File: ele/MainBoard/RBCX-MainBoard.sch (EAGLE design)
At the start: 311 parts, among them IC1 AMS1117-3.3, IC10 INA180A4, IC11 INA180A4, IC2 DRV8833PWP, IC3 INA180A4, IC4 INA180A4, IC5 DRV8833PWP, IC6 INA180A4, IC7 INA180A4, IC8 INA180A4, IC9 INA180A4, Q1 NCE20P45Q, Q10 2N7002, Q11 2N7002, Q2 NCE20P45Q, Q3 2N7002, Q4 2N7002, Q5 2N7002, Q6 2N7002, Q7 2N7002, Q8 2N7002, Q9 2N7002, SW1 CHOOSE_ME, SW2 CHOOSE_ME, SW3 CHOOSE_ME, SW4 CHOOSE_ME, SW5 CHOOSE_ME, SW6 CHOOSE_ME, U1 STM32F103VCT6, X1 POWER_OUT, X10 52745-3090, X11 52745-2090, X2 POWER_IN, Y1 5032/2P, Y2 3215_2P

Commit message: MainBoard: Add BOM, update parts value and package
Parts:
- removed C50: 10n, rcl_upravena:C-EUC0603
- removed C51: 1n, rcl_upravena:C-EUC0603
- removed C52, C54: 18p, rcl_upravena:C-EUC0603
- removed C53, C55: 6p, rcl_upravena:C-EUC0603
- removed C57: 10u, rcl_upravena:C-EUC0805
- removed JP56: ESP_I2C1, pinhead:PINHD-1X4
- removed JP57: ESP_SPI_AUX3, pinhead:PINHD-1X3
- removed JP58: +3V3STM, pinhead:PINHD-2X4
- removed JP59: ESP_I2C_AUX1, pinhead:PINHD-1X3
- removed JP60: +3V3, pinhead:PINHD-2X4
- removed JP61: +5V, pinhead:PINHD-2X4
- removed JP62: ESP_I2C2, pinhead:PINHD-1X4
- removed JP63: VCC, pinhead:PINHD-2X4
- removed JP64: ESP_I2C_AUX2, pinhead:PINHD-1X3
- removed JP66: ILED, pinhead:PINHD-1X3
- removed R119, R120, R125, R131, R132, R134: 4k7, rcl_upravena:R-EU_R0402
- removed R121, R122, R123, R124, R127, R128, R133: 180R, rcl_upravena:R-EU_R0402
- removed R126, R129: 100k, rcl_upravena:R-EU_R0402
- removed SJ8: (no value), jumper:SJ2W
- added C1, C6: 10u, rcl_upravena:C-EUC0805
- added C11: 10n, rcl_upravena:C-EUC0402
- added C17: 2u2, rcl_upravena:C-EUC0603
- added C23: 220u, rcl_upravena:CPOL-EUE5-10.5
- added C24, C25, C26: 100n, rcl_upravena:C-EUC0402
- added JP22: BOOT_SW, pinhead:PINHD-1X2
- added JP25: UTS2, pinhead:PINHD-1X4
- added JP31: ESP_SPI1, pinhead:PINHD-1X6
- added JP33: ESP_UART_AUX, pinhead:PINHD-1X3
- added JP34: ESP_I2C_AUX1_5V, pinhead:PINHD-1X3
- added JP35: ESP_SPI_AUX1, pinhead:PINHD-1X3
- added JP36: ESP_I2C2_5V, pinhead:PINHD-1X4
- added JP37: ESP_SPI2, pinhead:PINHD-1X6
- added JP38: ESP_UCOM, pinhead:PINHD-1X4
- added JP39: ESP_I2C_AUX2_5V, pinhead:PINHD-1X3
- added R70, R71, R72, R73, R74, R82, R84, R85, R89, R90, R91, R92, R94, R95: 330R, rcl_upravena:R-EU_R0402
- added R86: 4k7, rcl_upravena:R-EU_R0402
- added SJ3: (no value), jumper:SJ2W
- C10: value 2u2 -> 10u; device rcl_upravena:C-EUC0603 -> rcl_upravena:C-EUC0805; VOLTAGE 16V -> 25V
- C12: value 10u -> 2u2; device rcl_upravena:C-EUC0805 -> rcl_upravena:C-EUC0603; VOLTAGE 25V -> 16V
- C13, C19: device rcl_upravena:C-EUC0603 -> rcl_upravena:C-EUC0402; VOLTAGE 25V -> 16V
- C14: value 2u2 -> 100n; device rcl_upravena:C-EUC0805 -> rcl_upravena:C-EUC0402
- C15, C32, C33, C34, C44: value 100n -> 10u; device rcl_upravena:C-EUC0603 -> rcl_upravena:C-EUC0805; VOLTAGE 16V -> 25V
- C16: value 100n -> 10n; device rcl_upravena:C-EUC0603 -> rcl_upravena:C-EUC0402; VOLTAGE 16V -> 25V
- C18: value 10u -> 100n; device rcl_upravena:C-EUC0805 -> rcl_upravena:C-EUC0402; VOLTAGE 25V -> 16V
- C2: value 22u -> 10u; device rcl_upravena:CPOL-EUB/3528-21R -> rcl_upravena:C-EUC0805; DIELECTRIC (none) -> X5R; VOLTAGE 16V -> 25V
- C20: value 2u2 -> 220u; device rcl_upravena:C-EUC0805 -> rcl_upravena:CPOL-EUE5-10.5; DIELECTRIC X5R -> (none)
- C21, C22: value 100n -> 220u; device rcl_upravena:C-EUC0603 -> rcl_upravena:CPOL-EUE5-10.5; DIELECTRIC X5R -> (none)
- C27, C43: value 220u -> 100n; device rcl_upravena:CPOL-EUE5-10.5 -> rcl_upravena:C-EUC0402; DIELECTRIC (none) -> X5R
- C28, C29, C30: value 220u -> 1u; device rcl_upravena:CPOL-EUE5-10.5 -> rcl_upravena:C-EUC0402; DIELECTRIC (none) -> X5R
- C3, C42: VOLTAGE 16V -> 25V
- C31: value 100n -> 1u; device rcl_upravena:C-EUC0603 -> rcl_upravena:C-EUC0402
- C35: value 1u -> 10u; device rcl_upravena:C-EUC0603 -> rcl_upravena:C-EUC0805; VOLTAGE 16V -> 25V
- C36: value 1u -> 220u; device rcl_upravena:C-EUC0603 -> rcl_upravena:CPOL-EUE5-10.5; DIELECTRIC X5R -> (none)
- C37, C38: value 1u -> 100n; device rcl_upravena:C-EUC0603 -> rcl_upravena:C-EUC0402
- C39, C40, C41: value 10u -> 100n; device rcl_upravena:C-EUC0805 -> rcl_upravena:C-EUC0402
- C45, C47: value 100n -> 18p; device rcl_upravena:C-EUC0603 -> rcl_upravena:C-EUC0402; DIELECTRIC X5R -> np0; VOLTAGE 16V -> 50V
- C46, C48: value 100n -> 6.8p; device rcl_upravena:C-EUC0603 -> rcl_upravena:C-EUC0402; DIELECTRIC X5R -> np0; VOLTAGE 16V -> 50V
- C49: value 4u7 -> 10u; VOLTAGE 16V -> 25V
- C8: value 10u -> 1u; device rcl_upravena:C-EUC0805 -> rcl_upravena:C-EUC0402
- C9: value 1u -> 2u2
- IC3, IC4, IC6, IC7: DESCRIPTION PMIC - CURRENT & POWER MONITORS & REGULATORS 1 200 V/V ±0.1% 105KHZ -0.2V ~ 26V 2.7V ~ 5.5V SOT-23-5 ROHS -> PMIC - CURRENT & POWER MONITORS & REGULATORS 1 200 V/V ±0.1% 105KHZ -0.2V ~ 26V 2.7V ~ 5.5V SOT-23-5 ROHS
- JP1: value IM7_EN -> IM1_EN
- JP10: value IM1_EN -> IM2_EN
- JP11: value IM2_EN -> IM3_EN
- JP12: value IM3_EN -> IM4_EN
- JP13: value IM4_EN -> IM5_EN
- JP15: value SERVO1 -> SERVO2
- JP16: value SERVO1 -> SERVO3
- JP17: value SERVO1 -> SERVO4
- JP26: value BOOT_SW -> EXPANDER_UART; device pinhead:PINHD-1X2 -> pinhead:PINHD-1X3
- JP27: value UTS2 -> DEBUG
- JP28: value EXPANDER_UART -> UTS3; device pinhead:PINHD-1X3 -> pinhead:PINHD-1X4
- JP29: value DEBUG -> UTS4
- JP30: value UTS3 -> ESP_UART
- JP32: value UTS4 -> ESP_I2C1_5V
- JP43: value ESP_UART -> ESP_I2C1
- JP44: value ESP_SPI1 -> ESP_SPI_AUX3; device pinhead:PINHD-1X6 -> pinhead:PINHD-1X3
- JP45: value ESP_I2C1_5V -> +3V3STM; device pinhead:PINHD-1X4 -> pinhead:PINHD-2X4
- JP46: value ESP_UART_AUX -> ESP_I2C_AUX1
- JP47: value ESP_I2C_AUX1_5V -> +3V3; device pinhead:PINHD-1X3 -> pinhead:PINHD-2X4
- JP48: value ESP_SPI_AUX1 -> +5V; device pinhead:PINHD-1X3 -> pinhead:PINHD-2X4
- JP49: value ESP_I2C2_5V -> ESP_I2C2
- JP50: value ESP_SPI2 -> VCC; device pinhead:PINHD-1X6 -> pinhead:PINHD-2X4
- JP51: value ESP_UCOM -> ESP_I2C_AUX2; device pinhead:PINHD-1X4 -> pinhead:PINHD-1X3
- JP52: value ESP_I2C_AUX2_5V -> ILED
- LED1: value GREEN -> green; device led:LEDSML0603 -> led:LEDCHIP-LED0603
- LED2: value GREEN -> yellow; device led:LEDSML0603 -> led:LEDCHIP-LED0603
- LED3: value GREEN -> red; device led:LEDSML0603 -> led:LEDCHIP-LED0603
- LED4: value GREEN -> blue; device led:LEDSML0603 -> led:LEDCHIP-LED0603
- LED5: value green -> red
- LED6: value yellow -> red
- LED8: value blue -> red
- R10, R11: value 4k7 -> 10k
- R100, R101, R111, R112, R113, R87: value 180R -> 4k7
- R102, R103, R104, R108, R109, R114, R47, R48, R49, R50, R51, R64, R65, R67, R69, R75, R76, R77, R78, R79, R80, R81, R83, R88, R93, R96, R99: value 180R -> 330R
- R105: value 4k7 -> 330R
- R107, R110, R62, R63: value 180R -> 100k
- R13: value 4k7 -> 2k2
- R14, R15, R40: value 2k2 -> 1k
- R18, R19: value 8m -> 2k2; device rcl_upravena:R-EU_R1206S -> rcl_upravena:R-EU_R0402
- R2, R5: value 2M -> 10k
- R20, R21, R41: value 2k2 -> 5m; device rcl_upravena:R-EU_R0402 -> rcl_upravena:R-EU_R1206S
- R24, R25: value 10k -> 2k2
- R26, R27: value 8m -> 10k; device rcl_upravena:R-EU_R1206S -> rcl_upravena:R-EU_R0402
- R28, R29: value 0R -> 5m
- R32: value 1k -> 0R; device rcl_upravena:R-EU_R0402 -> rcl_upravena:R-EU_R1206S
- R33: value 5m -> 0R
- R4: value 100k -> 1M
- R44: device rcl_upravena:R-EU_R0603 -> rcl_upravena:R-EU_R0402
- R45, R46: value 180R -> 2k2
- R53: value 330R -> 100k
- R6: value 24k -> 100k
- R60, R61: value 100k -> 330R
- R66: value 10k -> 330R; device rcl_upravena:R-EU_R0603 -> rcl_upravena:R-EU_R0402
- R68: value 10k -> 330R
- R7: value 5k6 -> 1M
- R8: value 10k -> 24k
- R9: value 10k -> 5k6
- X5: value (none) -> uUSB
- renumbered J1 to X5, JP53 to JP40, JP54 to JP41, JP55 to JP42, R115 to R96, R116 to R97, R117 to R98, R118 to R99, SJ10 to SJ6, SJ11 to SJ7, SJ9 to SJ5, SW1 to S1, SW2 to S2, SW3 to S3, SW4 to S4, SW5 to S5, SW6 to S6, U1 to IC12, X10 to X3, X11 to X4
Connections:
- net +3V3: now also JP33.3, JP35.3, JP37.1, JP43.1, JP44.3, JP47.1, JP47.3, JP47.5, JP47.7, JP49.1, JP51.3, LED8.A, R100.2, R106.1, R107.1, R110.1, R111.1, R112.2, R86.2, SJ4.1; no longer JP48.3, JP50.1, JP56.1, JP57.3, JP59.3, JP60.1, JP60.3, JP60.5, JP60.7, JP62.1, JP64.3, LED4.A, R105.2, R119.2, R125.1, R126.1, R129.1, R131.1, R134.2, SJ8.1
- net +3V3S: now also C13.1, C14.1, C18.1, C19.1, C2.2, C24.1, C25.1, C26.1, C27.1, C3.2, C37.2, C38.2, C39.2, C40.2, C41.2, C42.2, C43.2, JP22.1, JP27.1, JP45.1, JP45.3, JP45.5, JP45.7, LED7.A, R5.2; no longer C15.1, C16.1, C2.+, C21.1, C22.1, C31.1, C32.1, C33.1, C34.1, C45.2, C46.2, C47.2, C48.2, C49.2, C50.2, C51.2, JP26.1, JP29.1, JP58.1, JP58.3, JP58.5, JP58.7, LED3.A, R3.2
- net +5V: now also JP25.1, JP28.1, JP29.1, JP48.1, JP48.3, JP48.5, JP48.7, JP52.1, LED6.A, R113.2, R30.1, SJ4.3; no longer JP27.1, JP30.1, JP32.1, JP61.1, JP61.3, JP61.5, JP61.7, JP66.1, LED2.A, R132.2, R28.1, SJ8.3
- net 3V3_IN: now also C1.2; no longer C3.2
- net BOOT0: now also JP22.2, R63.1; no longer JP26.2, R60.1
- net BOOT1_PULL-DOWN: now also R62.1; no longer R61.1
- net BUTTON-1: now also R47.2; no longer R45.2
- net BUTTON-2: now also R48.2; no longer R46.2
- net BUTTON-3: now also R49.2; no longer R47.2
- net BUTTON-4: now also R50.2; no longer R48.2
- net BUTTON-OFF: now also R51.2; no longer R49.2
- net BUTTON1: now also R47.1, R62.2; no longer R45.1, R61.2
- net BUTTON2: now also R48.1; no longer R46.1
- net BUTTON3: now also R49.1; no longer R47.1
- net BUTTON4: now also R50.1; no longer R48.1
- net BUTTON_OFF: now also R51.1; no longer R49.1
- net BUZZER: now also R52.1; no longer R50.1
- net BUZZER-GATE: now also R52.2, R53.1; no longer R50.2, R51.1
- net DEBUG-RX: now also JP27.3, R74.2; no longer JP29.3, R79.2
- net DEBUG-TX: now also JP27.4, R75.2, SJ3.1; no longer JP29.4, R80.2, SJ4.1
- net DEBUG_RX: now also R74.1; no longer R79.1
- net DEBUG_TX: now also R75.1; no longer R80.1
- net ENC1A: now also R16.1; no longer R14.1
- net ENC1B: now also R17.1; no longer R15.1
- net ENC2A: now also R18.1; no longer R16.1
- net ENC2B: now also R19.1; no longer R17.1
- net ENC3-SWO: now also SJ3.3; no longer SJ4.3
- net ENC3A: now also R22.1; no longer R20.1
- net ENC3B/SWO: now also R23.1; no longer R21.1
- net ENC4A: now also R24.1; no longer R22.1
- net ENC4B: now also R25.1; no longer R23.1
- net ENC_1A: now also R16.2; no longer R14.2
- net ENC_1B: now also R17.2; no longer R15.2
- net ENC_2A: now also R18.2; no longer R16.2
- net ENC_2B: now also R19.2; no longer R17.2
- net ENC_3A: now also R22.2; no longer R20.2
- net ENC_3B: now also R23.2; no longer R21.2
- net ENC_4A: now also R24.2; no longer R22.2
- net ENC_4B: now also R25.2; no longer R23.2
- net ESP-EN: now also R80.2; no longer R93.2
- net ESP-I2C-PWR: now also JP32.1, JP34.3, JP36.1, JP39.3, R101.2, R87.2, SJ4.2; no longer JP45.1, JP47.3, JP49.1, JP52.3, R106.2, R120.2, SJ8.2
- net ESP-I2C-SCL: now also JP43.3, JP49.3, R86.1, R92.2; no longer JP56.3, JP62.3, R105.1, R111.2
- net ESP-I2C-SCL-5V: now also JP32.3, JP36.3, R87.1; no longer JP45.3, JP49.3, R106.1
- net ESP-I2C-SDA: now also JP43.4, JP49.4; no longer JP56.4, JP62.4
- net ESP-I2C-SDA-5V: now also JP32.4, JP36.4; no longer JP45.4, JP49.4
- net ESP-SPI-!CS1: now also JP31.6, R94.2; no longer JP44.6, R113.2
- net ESP-SPI-!CS2: now also JP37.6, R102.2; no longer JP50.6, R121.2
- net ESP-SPI-!CS3: now also R109.2; no longer R128.2
- net ESP-SPI-MISO: now also JP31.4, JP37.4, R90.2; no longer JP44.4, JP50.4, R109.2
- net ESP-SPI-MOSI: now also JP31.3, JP37.3, R88.2; no longer JP44.3, JP50.3, R107.2
- net ESP-SPI-SCK: now also JP31.5, JP37.5, R93.2; no longer JP44.5, JP50.5, R112.2
- net ESP-USART-RX: now also JP30.3, R89.2; no longer JP43.3, R108.2
- net ESP-USART-TX: now also JP30.4, R91.2; no longer JP43.4, R110.2
- net ESP_+5V: now also C49.2; no longer C57.2
- net ESP_BOOT: now also R81.2; no longer R100.2
- net ESP_BOOT/I_LED: now also R114.1, R81.1; no longer R100.1, R133.1
- net ESP_COM_RX: now also R72.1, R82.2; no longer R101.2, R77.1
- net ESP_COM_TX: now also R73.1, R83.2; no longer R102.2, R78.1
- net ESP_EN: now also R80.1; no longer R93.1
- net ESP_PROG_RX: now also R84.2; no longer R103.2
- net ESP_PROG_TX: now also R85.2; no longer R104.2
- net ESP_SPI_PWR: now also JP31.1; no longer JP44.1
- net ESP_UCOM_PWR: now also JP38.1; no longer JP51.1
- net ESP_USART_PWR: now also JP30.1; no longer JP43.1
- net EXPANDER-UART-RX: now also JP26.1, R72.2; no longer JP28.1, R77.2
- net EXPANDER-UART-TX: now also JP26.2, R73.2; no longer JP28.2, R78.2
- net EXPANDER_RX: now also R83.1; no longer R102.1
- net EXPANDER_TX: now also R82.1; no longer R101.1
- net GND: now also C1.1, C13.2, C17.2, C19.2, C2.1, C20.-, C21.-, C22.-, C23.-, C24.2, C25.2, C26.2, C27.2, C28.2, C29.2, C30.2, C32.1, C33.1, C34.1, C35.1, C36.-, C37.1, C38.1, C43.1, C7.2, JP25.4, JP26.3, JP27.2, JP28.4, JP29.4, JP30.2, JP31.2, JP32.2, JP33.2, JP34.2, JP35.2, JP36.2, JP37.2, JP38.2, JP39.2, JP45.4, JP45.6, JP45.8, JP47.4, JP47.6, JP47.8, JP48.4, JP48.6, JP48.8, JP50.4, JP50.6, JP50.8, JP52.3, LED1.C, LED2.C, LED3.C, LED4.C, R14.1, R15.1, R2.1, R20.1, R21.1, R28.1, R29.1, R53.2, R6.1, R63.2, R7.1; no longer C16.2, C2.-, C20.2, C21.2, C22.2, C27.-, C28.-, C29.-, C30.-, C32.2, C33.2, C34.2, C35.2, C36.2, C37.2, C38.2, C43.-, C50.1, C51.1, C52.1, C53.1, C54.1, C55.1, C57.1, JP27.4, JP28.3, JP29.2, JP30.4, JP32.4, JP52.2, JP56.2, JP57.2, JP58.2, JP58.4, JP58.6, JP58.8, JP59.2, JP60.2, JP60.4, JP60.6, JP60.8, JP61.2, JP61.4, JP61.6, JP61.8, JP62.2, JP63.2, JP63.4, JP63.6, JP63.8, JP64.2, JP66.3, LED5.C, LED6.C, LED7.C, LED8.C, R18.1, R19.1, R24.1, R25.1, R4.1, R5.1, R51.2, R60.2, R68.1, R8.1, R9.1
- net GPIO-1: now also JP38.3, R104.2; no longer JP51.3, R123.2
- net GPIO-2: now also JP38.4, R105.2; no longer JP51.4, R124.2
- net GPIO-3: now also JP35.1; no longer JP48.1
- net GPIO-4: now also JP46.1, R100.1, R103.2; no longer JP59.1, R119.1, R122.2
- net GPIO-4-5V: now also JP34.1, R101.1; no longer JP47.1, R120.1
- net GPIO-5: now also R108.2; no longer R127.2
- net GPIO-6: now also JP33.1, R95.2; no longer JP46.1, R114.2
- net GPIO1: now also R104.1; no longer R123.1
- net GPIO2: now also R105.1; no longer R124.1
- net GPIO4: now also R103.1; no longer R122.1
- net GPIO5: now also R108.1; no longer R127.1
- net GPIO6: now also R95.1; no longer R114.1
- net I2C_SCL: now also R92.1; no longer R111.1
- net ILED: now also R112.1, R114.2; no longer R133.2, R134.1
- net ILED-5V: now also JP52.2, R113.1; no longer JP66.2, R132.1
- net IN1: now also R107.2; no longer R126.2
- net IN2: now also JP44.1, R110.2; no longer JP57.1, R129.2
- net IN3: now also R106.2; no longer R125.2
- net IN3-5V: now also JP39.1; no longer JP52.1
- net IN4: now also JP51.1, R111.2; no longer JP64.1, R131.2
- net IN4_A: now also R27.2; no longer R25.2
- net IN4_B: now also R26.2; no longer R24.2
- net INTELLIGENT_SERVO: now also R46.1; no longer R44.1
- net ISERVO: now also R46.2; no longer R44.2
- net LED-1: now also R58.2; no longer R56.2
- net LED-2: now also R59.2; no longer R57.2
- net LED-3: now also R60.2; no longer R58.2
- net LED-4: now also R61.2; no longer R59.2
- net LED1: now also R54.1, R58.1; no longer R52.1, R56.1
- net LED2: now also R55.1, R59.1; no longer R53.1, R57.1
- net LED3: now also R56.1, R60.1; no longer R54.1, R58.1
- net LED4: now also R57.1, R61.1; no longer R55.1, R59.1
- net LED_1: now also LED1.A, R54.2; no longer LED5.A, R52.2
- net LED_2: now also LED2.A, R55.2; no longer LED6.A, R53.2
- net LED_3: now also LED3.A, R56.2; no longer LED7.A, R54.2
- net LED_4: now also LED4.A, R57.2; no longer LED8.A, R55.2
- net M1GND: now also R20.2; no longer R18.2
- net M2GND: now also R21.2; no longer R19.2
- net M3GND: now also R28.2; no longer R26.2
- net M4GND: now also R29.2; no longer R27.2
- net N$11: now also C6.2, R4.1; no longer C7.2, R2.1
- net NRST: now also R68.1; no longer R67.1
- net NRST_: now also R68.2; no longer R67.2
- net OSC32_IN: now also C46.2; no longer C53.2
- net OSC32_OUT: now also C48.2; no longer C55.2
- net OSC_IN: now also C45.2; no longer C52.2
- net OSC_OUT: now also C47.2; no longer C54.2
- net POWER: now also C7.1, R5.1, R7.2; no longer C8.1, R3.1, R5.2
- net PROT_GATE: now also R2.2; no longer R68.2
- net PWRLED_VCC: now also LED5.C, R12.2; no longer LED1.C, R10.2
- net PWRLED_VCC1: now also LED6.C, R13.2; no longer LED2.C, R11.2
- net PWRLED_VCC2: now also LED7.C, R14.2; no longer LED3.C, R12.2
- net PWRLED_VCC3: now also LED8.C, R15.2; no longer LED4.C, R13.2
- net PWRSW: now also C6.1, R3.1, R4.2; no longer C7.1, R2.2, R66.1
- net PWRSW_GATE: now also R3.2; no longer R66.2
- net PWR_BTN: now also R6.2; no longer R4.2
- net SERVO1: now also R42.1; no longer R40.1
- net SERVO1PWR: now also R30.2, R31.1; no longer R28.2, R29.1
- net SERVO1_PWR: now also C20.+, R35.2; no longer C27.+, R33.2
- net SERVO2: now also R43.1; no longer R41.1
- net SERVO2PWR: now also R31.2, R32.1; no longer R29.2, R30.1
- net SERVO2_PWR: now also C21.+, R37.2; no longer C28.+, R35.2
- net SERVO3: now also R44.1; no longer R42.1
- net SERVO3PWR: now also R32.2, R33.1; no longer R30.2, R31.1
- net SERVO3_PWR: now also C22.+, R39.2; no longer C29.+, R37.2
- net SERVO4: now also R45.1; no longer R43.1
- net SERVO4PWR: now also R33.2; no longer R31.2
- net SERVO4_PWR: now also C23.+, R41.2; no longer C30.+, R39.2
- net SERVO_1: now also R42.2; no longer R40.2
- net SERVO_1_PWR: now also C32.2, R35.1; no longer C39.2, R33.1
- net SERVO_2: now also R43.2; no longer R41.2
- net SERVO_2_PWR: now also C33.2, R37.1; no longer C40.2, R35.1
- net SERVO_3: now also R44.2; no longer R42.2
- net SERVO_3_PWR: now also C34.2, R39.1; no longer C41.2, R37.1
- net SERVO_4: now also R45.2; no longer R43.2
- net SERVO_4_PWR: now also C35.2, R41.1; no longer C42.2, R39.1
- net SI1: now also C28.1, R34.1; no longer C35.1, R32.1
- net SI2: now also C29.1, R36.1; no longer C36.1, R34.1
- net SI3: now also C30.1, R38.1; no longer C37.1, R36.1
- net SI4: now also C31.1, R40.1; no longer C38.1, R38.1
- net SI_1: now also R34.2; no longer R32.2
- net SI_2: now also R36.2; no longer R34.2
- net SI_3: now also R38.2; no longer R36.2
- net SI_4: now also R40.2; no longer R38.2
- net SPI_!SS1: now also R94.1; no longer R113.1
- net SPI_!SS2: now also R102.1; no longer R121.1
- net SPI_!SS3: now also R109.1; no longer R128.1
- net SPI_MISO: now also R90.1; no longer R109.1
- net SPI_MOSI: now also R88.1; no longer R107.1
- net SPI_SCK: now also R93.1; no longer R112.1
- net SWCLK: now also R65.1; no longer R63.1
- net SWCLK_: now also R65.2; no longer R63.2
- net SWDIO: now also R67.1; no longer R65.1
- net SWDIO_: now also R67.2; no longer R65.2
- net SWO: now also SJ3.2; no longer SJ4.2
- net UART2_RX: now also R89.1; no longer R108.1
- net UART2_TX: now also R91.1; no longer R110.1
- net UART_RX: now also R85.1; no longer R104.1
- net UART_TX: now also R84.1; no longer R103.1
- net UTS1-ECHO: now also R66.2; no longer R64.2
- net UTS1-TRIG: now also R64.2; no longer R62.2
- net UTS1_ECHO: now also R66.1; no longer R64.1
- net UTS1_TRIG: now also R64.1; no longer R62.1
- net UTS2-ECHO: now also JP25.3, R71.2; no longer JP27.3, R76.2
- net UTS2-TRIG: now also JP25.2, R70.2; no longer JP27.2, R75.2
- net UTS2_ECHO: now also R71.1; no longer R76.1
- net UTS2_TRIG: now also R70.1; no longer R75.1
- net UTS3-ECHO: now also JP28.3, R77.2; no longer JP30.3, R83.2
- net UTS3-TRIG: now also JP28.2, R76.2; no longer JP30.2, R81.2
- net UTS3_ECHO: now also R77.1; no longer R83.1
- net UTS3_TRIG: now also R76.1; no longer R81.1
- net UTS4-ECHO: now also JP29.3, R79.2; no longer JP32.3, R88.2
- net UTS4-TRIG: now also JP29.2, R78.2; no longer JP32.2, R87.2
- net UTS4_ECHO: now also R79.1; no longer R88.1
- net UTS4_TRIG: now also R78.1; no longer R87.1
- net VBAT/2: now also R9.2; no longer R7.2
- net VCC: now also C10.1, C11.1, C15.1, C16.1, C36.+, JP50.1, JP50.3, JP50.5, JP50.7, LED5.A, R8.2; no longer C12.1, C13.1, C18.1, C19.1, C43.+, JP63.1, JP63.3, JP63.5, JP63.7, LED1.A, R6.2
- net VCP12: now also C11.2; no longer C13.2
- net VCP34: now also C16.2; no longer C19.2
- net VINT12: now also C12.1; no longer C14.1
- net VINT34: now also C17.1; no longer C20.1
- net V_BAT: now also C8.1, R10.2, R8.1; no longer C9.1, R6.1, R8.2
- net V_BAT/2: now also C9.1, R11.2, R9.1; no longer C10.1, R7.1, R9.2

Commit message: MainBoardBRD: routing...
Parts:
- added X6: M1, con-wago-508:W237-02P
- added X7: M2, con-wago-508:W237-02P
- added X8: M3, con-wago-508:W237-02P
- added X9: M4, con-wago-508:W237-02P
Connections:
- net M1A: now also X6-1.KL
- net M1B: now also X6-2.KL
- net M2A: now also X7-1.KL
- net M2B: now also X7-2.KL
- net M3A: now also X8-1.KL
- net M3B: now also X8-2.KL
- net M4A: now also X9-1.KL
- net M4B: now also X9-2.KL

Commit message: MainBoardBRD: routing...
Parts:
- added JP53: ESP32_JTAG, pinhead:PINHD-1X6
- added M1: DISPLAY-OLED-128X32, diy-modules:DISPLAY-OLED-128X32
- X3: value 52745-3090 -> 52559-3092; device con-molex:52745-3090 -> con-molex:52559-3092
- X4: value 52745-2090 -> 52559-2092; device con-molex:52745-2090 -> con-molex:52559-2092
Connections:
- net +3V3: now also JP53.5
- net EXPANDER_RX: now also JP53.2
- net GND: now also JP53.6
- net INTELLIGENT_SERVO: now also JP53.1
- net SPI_!SS2: now also JP53.4
- net SPI_!SS3: now also JP53.3
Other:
- note added: "GND"
- note added: "TCK"
- note added: "TDI"
- note added: "TDO"
- note added: "TMS"

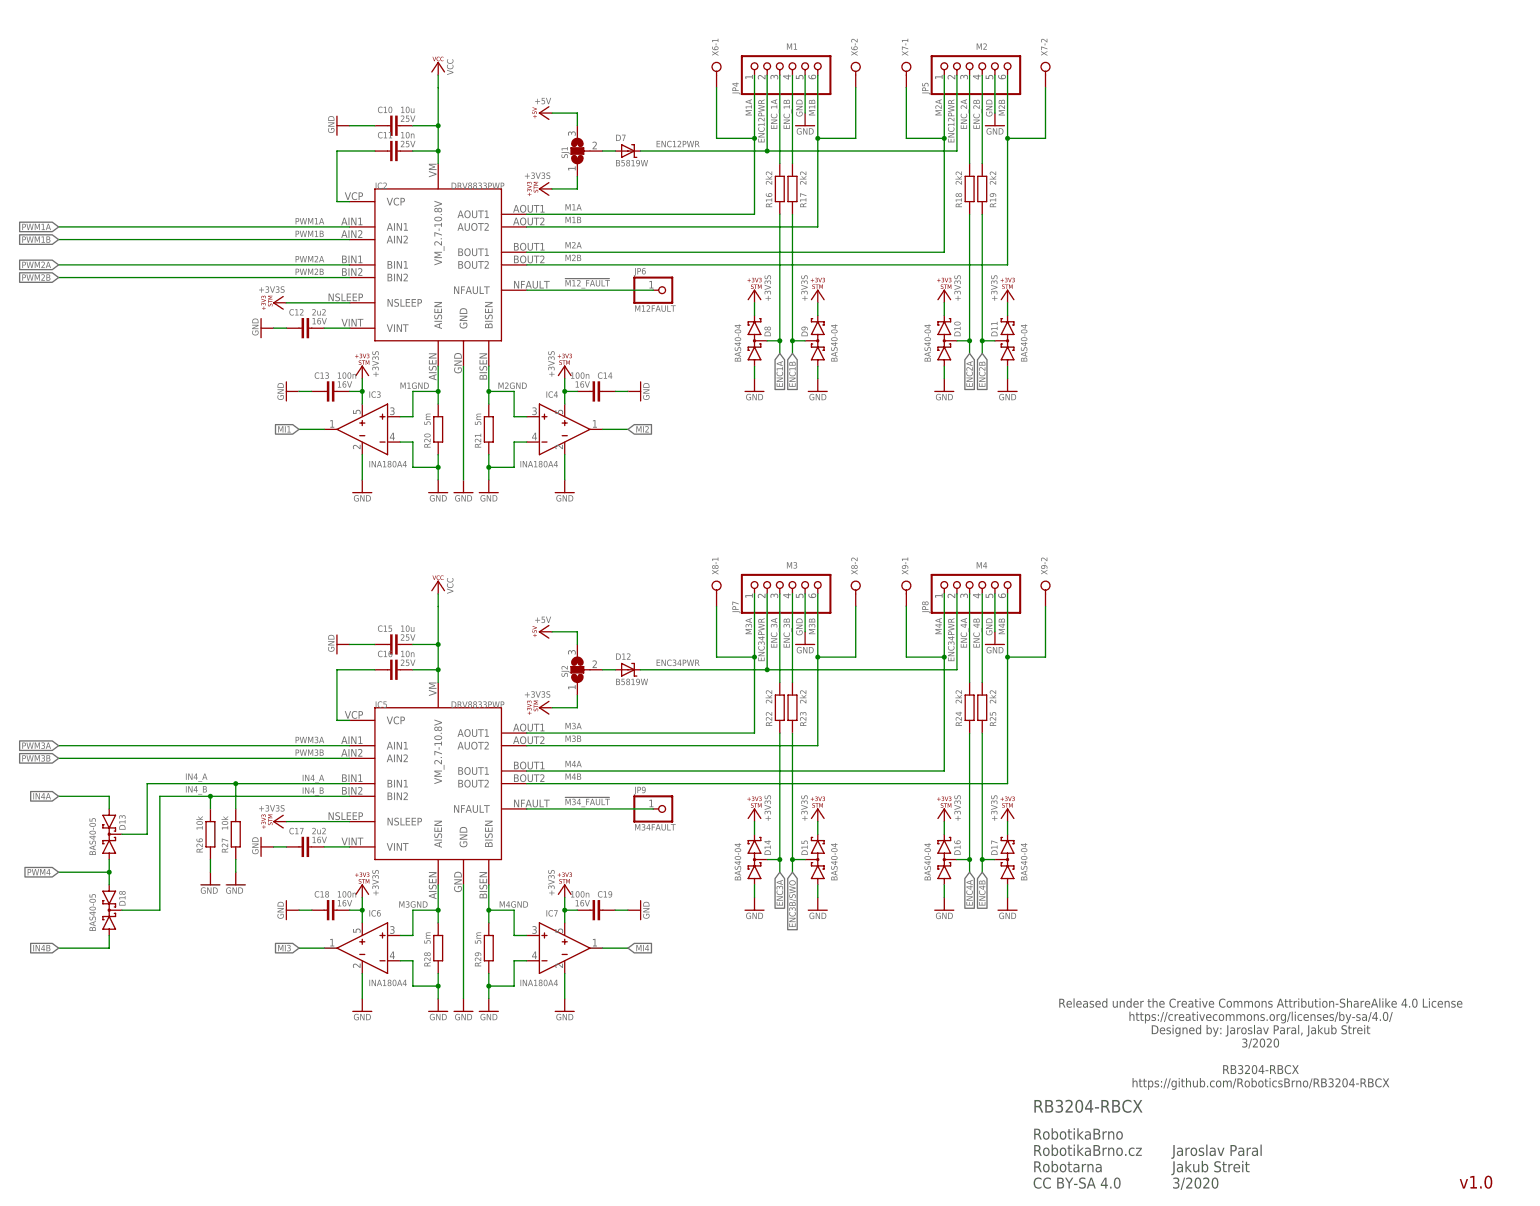
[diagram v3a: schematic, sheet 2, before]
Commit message: MainBoardBRD: change top side SMD parts footprint according IPC-7351 (using Library Expert Pro (2019.7) )
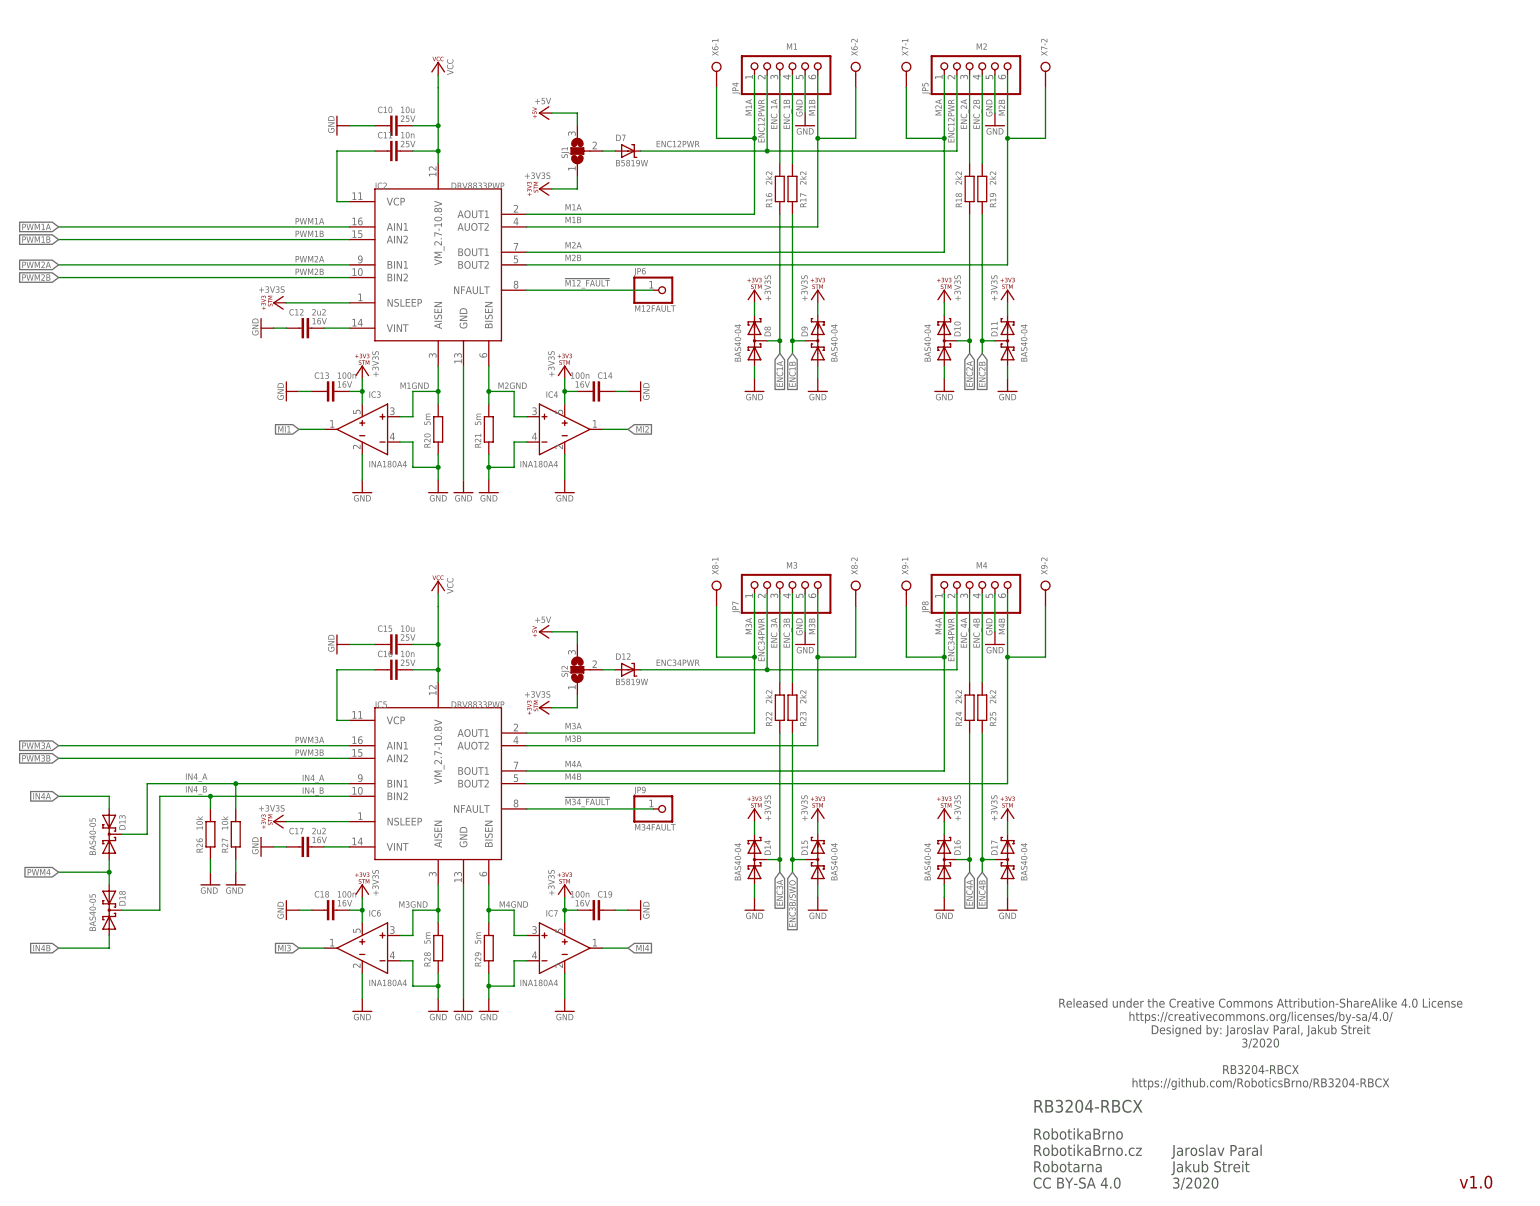
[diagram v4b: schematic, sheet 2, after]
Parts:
- D1, D19, D2, D20, D21, D22, D29, D3, D4, D5, D6: device diode:BAT60JDO-214-AB -> diode:SHOTTKY-SMA
- IC1: device v-reg:LM317MSTT3 -> ams1117:AMS1117
- LED1, LED2, LED3, LED4, LED5, LED6, LED7, LED8: device led:LEDCHIP-LED0603 -> led:LEDCHIPLED_0603
- R20, R21, R28, R29, R30, R31, R32, R33, R35, R37, R39, R41: device rcl_upravena:R-EU_R1206S -> rcl_upravena:R-EU_R1206
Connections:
- net GND: now also IC1.GND; no longer IC1.ADJ
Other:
- moved on the sheet: IC2, IC5
